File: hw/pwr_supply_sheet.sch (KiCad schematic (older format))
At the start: 17 parts

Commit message: starting to redraw the pcb as a smaller (icu enclosure)
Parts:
- C201, C205: symbol 100nF -> kemet:100nF
- C202: symbol CAP_EEE-FK1H470P -> usevolt:CAP_EEE-FK1H470P
- C203: symbol 10nF -> kemet:10nF
- C204: symbol T491D226K035AT -> kemet:T491D226K035AT
- D201, D204: symbol DIODE_RS07J-GS18 -> usevolt:DIODE_RS07J-GS18
- D202, D205: symbol SCHOTTKY_DIODE_V40PW10C -> usevolt:SCHOTTKY_DIODE_V40PW10C
- D203: symbol DIODE_TVS_SMBJ33A-TRDO-214AA -> usevolt:DIODE_TVS_SMBJ33A-TRDO-214AA
- D206: symbol DIODE_TVS_TPSMD28A -> usevolt:DIODE_TVS_TPSMD28A
- F201: symbol FUSE_MC36211_350MA -> usevolt:FUSE_MC36211_350MA
- L201: symbol IND_744045210 -> usevolt:IND_744045210
- R201: symbol 10K -> yageo:10K
- R202: symbol 1K -> yageo:1K
- VR201: symbol LM2671SOIC8 -> usevolt:LM2671SOIC8
- VR202: symbol REG_MCP1700 -> usevolt:REG_MCP1700
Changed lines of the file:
@@
-EESchema Schematic File Version 2
-LIBS:esb-rescue
-LIBS:kemet
-LIBS:usevolt
-LIBS:wurth_elektronik_LED
-LIBS:power
-LIBS:yageo
+EESchema Schematic File Version 4
 LIBS:esb-cache
 EELAYER 26 0
@@
 VIN
 $Comp
-L FUSE_MC36211_350MA F201
+L usevolt:FUSE_MC36211_350MA F201
 U 1 1 57B8204F
 P 2500 3850
@@
 $EndComp
 $Comp
-L DIODE_TVS_SMBJ33A-TRDO-214AA D203
+L usevolt:DIODE_TVS_SMBJ33A-TRDO-214AA D203
 U 1 1 57B820C1
 P 2800 4050
@@
 $EndComp
 $Comp
-L 100nF C201
+L kemet:100nF C201
 U 1 1 57B8217A
 P 3400 3950
@@
 $EndComp
 $Comp
-L LM2671SOIC8 VR201
+L usevolt:LM2671SOIC8 VR201
 U 1 1 57B82261
 P 4850 4150
@@
 $EndComp
 $Comp
-L 10nF C203
+L kemet:10nF C203
 U 1 1 57B822C5
 P 5800 3950
@@
 $EndComp
 $Comp
-L DIODE_RS07J-GS18 D204
+L usevolt:DIODE_RS07J-GS18 D204
 U 1 1 57B82329
 P 6200 3950
@@
 $EndComp
 $Comp
-L 100nF C205
+L kemet:100nF C205
 U 1 1 57B82A3F
 P 8600 3950
@@
 $EndComp
 $Comp
-L +5V #PWR07
+L power:+5V #PWR07
 U 1 1 57B831F8
 P 6850 3600
@@
 $EndComp
 $Comp
-L +3V3 #PWR08
+L power:+3V3 #PWR08
 U 1 1 57B83259
 P 8600 3600
@@
 NoConn ~ 4550 4050
 $Comp
-L VDD #PWR09
+L power:VDD #PWR09
 U 1 1 57B9C56A
 P 3800 2100
@@
 $EndComp
 $Comp
-L PWR_FLAG #FLG010
+L power:PWR_FLAG #FLG010
 U 1 1 57B9C59C
 P 3800 2300
@@
 $EndComp
 $Comp
-L GND #PWR011
+L power:GND #PWR011
 U 1 1 57B9D351
 P 4300 2350
@@
 $EndComp
 $Comp
-L PWR_FLAG #FLG012
+L power:PWR_FLAG #FLG012
 U 1 1 57B9D3A1
 P 4300 2150
@@
 $EndComp
 $Comp
-L GND #PWR013
+L power:GND #PWR013
 U 1 1 57CF1F5E
 P 2800 5150
@@
 $EndComp
 $Comp
-L IND_744045210 L201
+L usevolt:IND_744045210 L201
 U 1 1 58945E39
 P 6500 3850
@@
 $EndComp
 $Comp
-L DIODE_RS07J-GS18 D201
+L usevolt:DIODE_RS07J-GS18 D201
 U 1 1 5896E2A2
 P 1900 3850
@@
 $EndComp
 $Comp
-L T491D226K035AT C204
+L kemet:T491D226K035AT C204
 U 1 1 597AF606
 P 6850 4050
@@
 $EndComp
 $Comp
-L REG_MCP1700 VR202
+L usevolt:REG_MCP1700 VR202
 U 1 1 597AF83E
 P 8000 3950
@@
 $EndComp
 $Comp
-L 10K R201
+L yageo:10K R201
 U 1 1 59B1277F
 P 1500 4350
@@
 $EndComp
 $Comp
-L 1K R202
+L yageo:1K R202
 U 1 1 59B12803
 P 1500 4750
@@
 $EndComp
 $Comp
-L GND #PWR014
+L power:GND #PWR014
 U 1 1 59B128CC
 P 1500 5000
@@
 VDD_SENSE
 $Comp
-L SCHOTTKY_DIODE_V40PW10C D202
+L usevolt:SCHOTTKY_DIODE_V40PW10C D202
 U 1 1 59B7B8B2
 P 2050 3250
@@
 $EndComp
 $Comp
-L SCHOTTKY_DIODE_V40PW10C D205
+L usevolt:SCHOTTKY_DIODE_V40PW10C D205
 U 1 1 59D9089A
 P 2050 2750
@@
 $EndComp
 $Comp
-L CAP_EEE-FK1H470P C202
+L usevolt:CAP_EEE-FK1H470P C202
 U 1 1 5A13B69C
 P 3800 4050
@@
 $EndComp
 $Comp
-L DIODE_TVS_TPSMD28A D206
+L usevolt:DIODE_TVS_TPSMD28A D206
 U 1 1 5A13BC8E
 P 2900 2950
@@
 $EndComp
 $Comp
-L GND #PWR015
+L power:GND #PWR015
 U 1 1 5A13BD77
 P 2900 3150

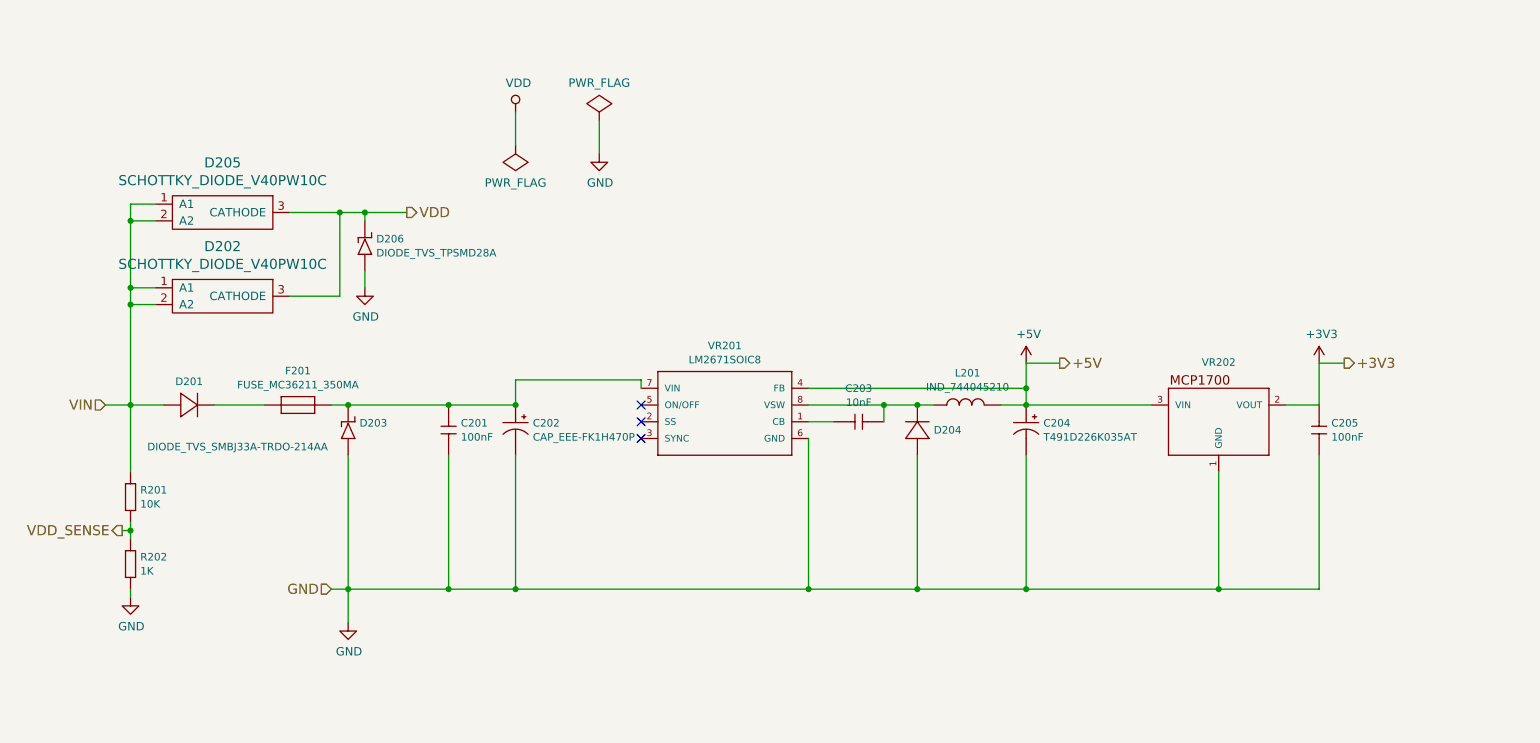
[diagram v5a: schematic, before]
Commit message: pump solenoid output working
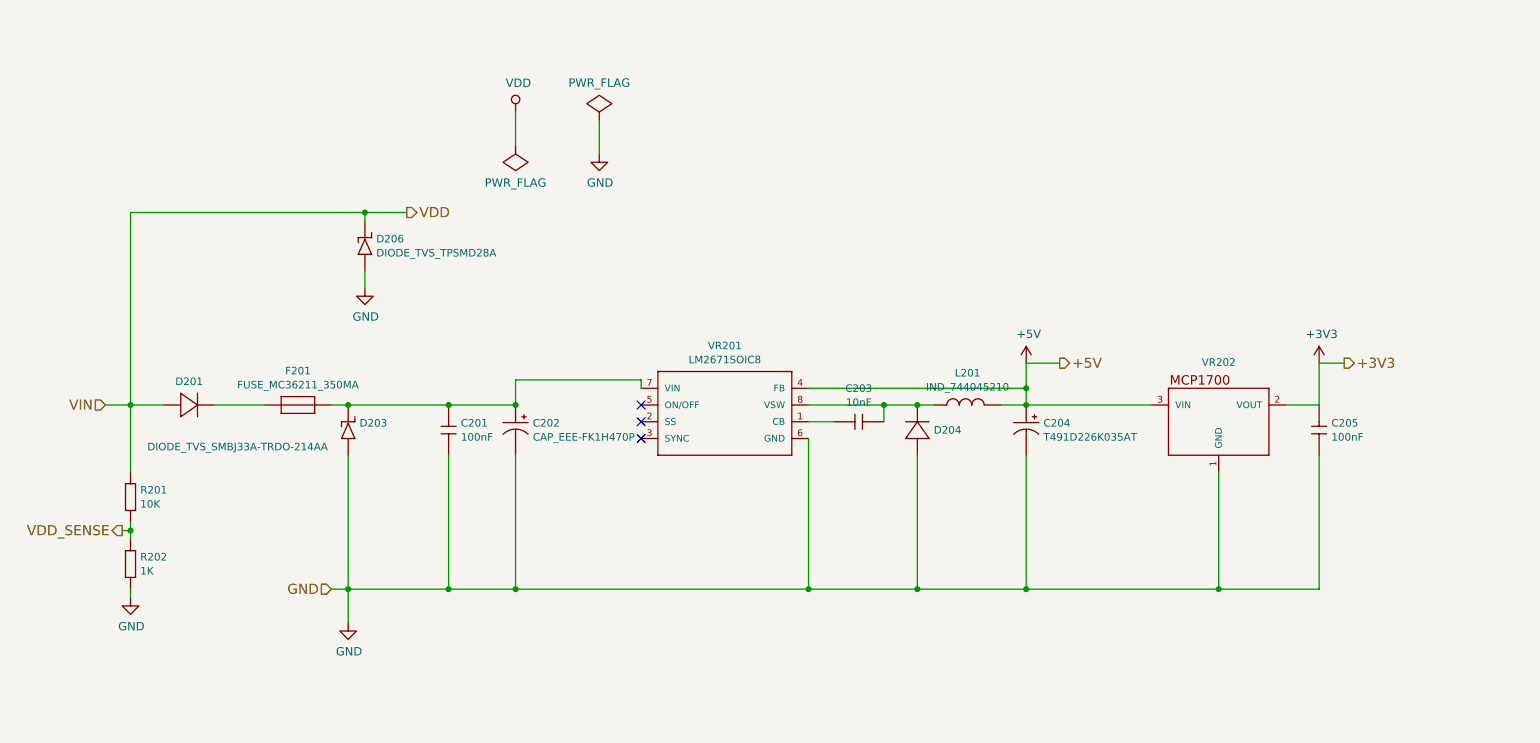
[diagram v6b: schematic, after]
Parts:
- removed D202, D205: SCHOTTKY_DIODE_V40PW10C, usevolt:SlimDPAK, symbol usevolt:SCHOTTKY_DIODE_V40PW10C
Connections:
- net VIN is gone; now on net VDD: D201.P$1 (P), R201.2 (R2)
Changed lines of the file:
@@
 VDD_SENSE
-$Comp
-L usevolt:SCHOTTKY_DIODE_V40PW10C D202
-U 1 1 59B7B8B2
-P 2050 3250
-F 0 "D202" H 2050 3597 60  0000 C CNN
-F 1 "SCHOTTKY_DIODE_V40PW10C" H 2050 3491 60  0000 C CNN
-F 2 "usevolt:SlimDPAK" H 1850 2900 60  0001 C CNN
-F 3 "http://www.farnell.com/datasheets/2245239.pdf?_ga=2.16591231.874534928.1505194133-1862443086.1504075057" H 1850 2900 60  0001 C CNN
-F 4 "2535169" H 2400 3850 60  0001 C CNN "1st Source Part Number"
-F 5 "Digikey" H 2500 3950 60  0001 C CNN "2nd Source"
-F 6 "Farnell" H 2300 3750 60  0001 C CNN "1st Source"
-F 7 "V40PW10CHM3/I" H 2200 3650 60  0001 C CNN "Manufacturer Part Number"
-F 8 "V40PW10CHM3/IGICT-ND" H 2600 4050 60  0001 C CNN "2nd Source Part Number"
-F 9 "VISHAY" H 2100 3550 60  0001 C CNN "Manufacturer"
-	1    2050 3250
-	1    0    0    -1
-$EndComp
-$Comp
-L usevolt:SCHOTTKY_DIODE_V40PW10C D205
-U 1 1 59D9089A
-P 2050 2750
-F 0 "D205" H 2050 3097 60  0000 C CNN
-F 1 "SCHOTTKY_DIODE_V40PW10C" H 2050 2991 60  0000 C CNN
-F 2 "usevolt:SlimDPAK" H 1850 2400 60  0001 C CNN
-F 3 "http://www.farnell.com/datasheets/2245239.pdf?_ga=2.16591231.874534928.1505194133-1862443086.1504075057" H 1850 2400 60  0001 C CNN
-F 4 "2535169" H 2400 3350 60  0001 C CNN "1st Source Part Number"
-F 5 "Digikey" H 2500 3450 60  0001 C CNN "2nd Source"
-F 6 "Farnell" H 2300 3250 60  0001 C CNN "1st Source"
-F 7 "V40PW10CHM3/I" H 2200 3150 60  0001 C CNN "Manufacturer Part Number"
-F 8 "V40PW10CHM3/IGICT-ND" H 2600 3550 60  0001 C CNN "2nd Source Part Number"
-F 9 "VISHAY" H 2100 3050 60  0001 C CNN "Manufacturer"
-	1    2050 2750
-	1    0    0    -1
-$EndComp
 $Comp
 L usevolt:CAP_EEE-FK1H470P C202
@@
 Connection ~ 3800 4950
 Wire Wire Line
-	2800 4150 2800 5150
+	2800 4150 2800 4950
 Connection ~ 3400 4950
 Connection ~ 2800 3850
@@
 	8600 3850 8400 3850
 Wire Wire Line
-	6700 3850 7600 3850
+	6700 3850 6850 3850
 Connection ~ 6850 3850
 Wire Wire Line
-	5550 3850 6300 3850
+	5550 3850 6000 3850
 Connection ~ 6200 3850
 Wire Wire Line
@@
 	5550 3750 6850 3750
 Wire Wire Line
-	6850 3600 6850 3850
+	6850 3600 6850 3750
 Connection ~ 6850 3750
 Wire Wire Line
-	1350 3850 1700 3850
+	1350 3850 1500 3850
 Wire Wire Line
 	3800 3700 4550 3700
@@
 Connection ~ 1500 3850
 Wire Wire Line
-	2700 3850 3800 3850
+	2700 3850 2800 3850
 Wire Wire Line
 	2000 3850 2300 3850
 Wire Wire Line
-	2700 4950 8600 4950
+	2700 4950 2800 4950
 Wire Wire Line
 	1500 5000 1500 4950
 Wire Wire Line
-	1500 4550 1500 4650
+	1500 4550 1500 4600
 Wire Wire Line
 	1500 4600 1450 4600
 Connection ~ 1500 4600
-Wire Wire Line
-	2750 3200 2450 3200
-Wire Wire Line
-	1500 2650 1500 4250
-Wire Wire Line
-	1500 3150 1650 3150
-Wire Wire Line
-	1650 3250 1500 3250
-Connection ~ 1500 3250
-Wire Wire Line
-	1500 2750 1650 2750
-Connection ~ 1500 3150
-Wire Wire Line
-	1500 2650 1650 2650
-Connection ~ 1500 2750
-Wire Wire Line
-	2450 2700 3150 2700
-Wire Wire Line
-	2750 2700 2750 3200
 Connection ~ 3800 3850
-Connection ~ 2750 2700
 Wire Wire Line
 	2900 2750 2900 2700
-Connection ~ 2900 2700
 Wire Wire Line
 	2900 3150 2900 3050
+Wire Wire Line
+	8000 4950 8600 4950
+Wire Wire Line
+	6850 4950 8000 4950
+Wire Wire Line
+	6200 4950 6850 4950
+Wire Wire Line
+	5550 4950 6200 4950
+Wire Wire Line
+	3800 4950 5550 4950
+Wire Wire Line
+	3400 4950 3800 4950
+Wire Wire Line
+	2800 3850 3400 3850
+Wire Wire Line
+	3400 3850 3800 3850
+Wire Wire Line
+	6850 3850 7600 3850
+Wire Wire Line
+	6200 3850 6300 3850
+Wire Wire Line
+	6000 3850 6200 3850
+Wire Wire Line
+	6850 3750 6850 3850
+Wire Wire Line
+	2800 4950 2800 5150
+Wire Wire Line
+	2800 4950 3400 4950
+Wire Wire Line
+	1500 3850 1700 3850
+Wire Wire Line
+	1500 3850 1500 4250
+Wire Wire Line
+	1500 4600 1500 4650
+Wire Wire Line
+	2900 2700 3150 2700
+Wire Wire Line
+	1500 2700 1500 3850
+Wire Wire Line
+	1500 2700 2900 2700
+Connection ~ 2900 2700
 $EndSCHEMATC

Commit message: pcb 5.2.0 ready for order, with radiator power output
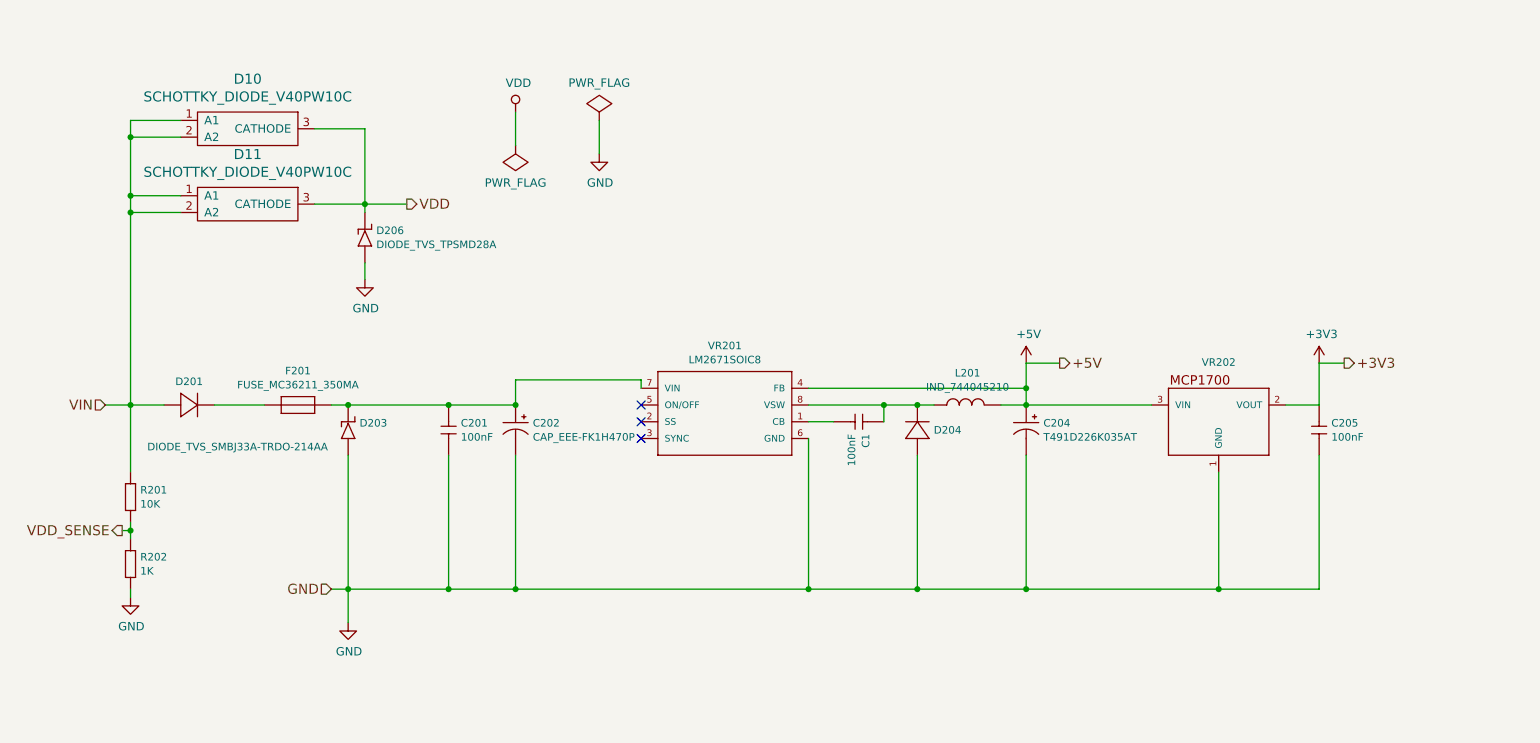
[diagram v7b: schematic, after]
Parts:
- removed C203: 10nF, kemet:0603, symbol kemet:10nF
- added C1: 100nF, kemet:0603, symbol kemet:100nF
- added D10, D11: SCHOTTKY_DIODE_V40PW10C, usevolt:SlimDPAK, symbol usevolt:SCHOTTKY_DIODE_V40PW10C
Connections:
- net VDD: now also D10.3 (CATHODE), D11.3 (CATHODE); no longer D201.P$1 (P), R201.2 (R2)
- net at VR201.1 (CB): now also C1.2 (C2)
- net at D204.P$2 (N), L201.1, VR201.8 (VSW): now also C1.1 (C1)
- new net VIN: D10.1 (A1), D10.2 (A2), D11.1 (A1), D11.2 (A2), D201.P$1 (P), R201.2 (R2)
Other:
- moved on the sheet: D206
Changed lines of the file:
@@
-$EndComp
-$Comp
-L kemet:10nF C203
-U 1 1 57B822C5
-P 5800 3950
-F 0 "C203" H 5850 4149 45  0000 C CNN
-F 1 "10nF" H 5850 4065 45  0000 C CNN
-F 2 "kemet:0603" H 5830 4100 20  0001 C CNN
-F 3 "http://www.farnell.com/datasheets/2064086.pdf?_ga=1.250530118.1948984246.1460023966" H 5704 3959 60  0001 C CNN
-F 4 "1457729" H 6104 4359 60  0001 C CNN "1st Source Part Number"
-F 5 "C0603C103J3GACTU" H 5904 4159 60  0001 C CNN "Manufacturer Part Number"
-F 6 "Farnell" H 6004 4259 60  0001 C CNN "1st Source"
-F 7 "KEMET" H 5804 4059 60  0001 C CNN "Manufacturer"
-	1    5800 3950
-	1    0    0    -1
 $EndComp
 $Comp
@@
 Text HLabel 8750 3600 2    60   Output ~ 0
 +3V3
-Text HLabel 3150 2700 2    60   Output ~ 0
+Text HLabel 3150 2650 2    60   Output ~ 0
 VDD
 Text HLabel 2700 4950 0    60   Input ~ 0
@@
 L usevolt:DIODE_TVS_TPSMD28A D206
 U 1 1 5A13BC8E
-P 2900 2950
-F 0 "D206" V 2992 2882 45  0000 R CNN
-F 1 "DIODE_TVS_TPSMD28A" V 2908 2882 45  0000 R CNN
-F 2 "usevolt:DO-214AB" H 2930 3100 20  0001 C CNN
-F 3 "http://www.littelfuse.com/~/media/electronics/datasheets/tvs_diodes/littelfuse_tvs_diode_tpsmd_datasheet.pdf.pdf" H 3010 2960 60  0001 C CNN
-F 4 "Digi-Key" H 3310 3260 60  0001 C CNN "1st Source"
-F 5 "Littlefuse" H 3110 3060 60  0001 C CNN "Manufacturer"
-F 6 "TPSMD28A" H 3210 3160 60  0001 C CNN "Manufacturer Part Number"
-F 7 "F6570CT-ND" H 3410 3360 60  0001 C CNN "1st Source Part Number"
-	1    2900 2950
+P 2900 2900
+F 0 "D206" V 2992 2832 45  0000 R CNN
+F 1 "DIODE_TVS_TPSMD28A" V 2908 2832 45  0000 R CNN
+F 2 "usevolt:DO-214AB" H 2930 3050 20  0001 C CNN
+F 3 "http://www.littelfuse.com/~/media/electronics/datasheets/tvs_diodes/littelfuse_tvs_diode_tpsmd_datasheet.pdf.pdf" H 3010 2910 60  0001 C CNN
+F 4 "Digi-Key" H 3310 3210 60  0001 C CNN "1st Source"
+F 5 "Littlefuse" H 3110 3010 60  0001 C CNN "Manufacturer"
+F 6 "TPSMD28A" H 3210 3110 60  0001 C CNN "Manufacturer Part Number"
+F 7 "F6570CT-ND" H 3410 3310 60  0001 C CNN "1st Source Part Number"
+	1    2900 2900
 	0    -1   -1   0
 $EndComp
@@
 L power:GND #PWR015
 U 1 1 5A13BD77
-P 2900 3150
-F 0 "#PWR015" H 2900 2900 50  0001 C CNN
-F 1 "GND" H 2905 2977 50  0000 C CNN
-F 2 "" H 2900 3150 50  0000 C CNN
-F 3 "" H 2900 3150 50  0000 C CNN
-	1    2900 3150
+P 2900 3100
+F 0 "#PWR015" H 2900 2850 50  0001 C CNN
+F 1 "GND" H 2905 2927 50  0000 C CNN
+F 2 "" H 2900 3100 50  0000 C CNN
+F 3 "" H 2900 3100 50  0000 C CNN
+	1    2900 3100
 	1    0    0    -1
 $EndComp
@@
 Connection ~ 3800 3850
 Wire Wire Line
-	2900 2750 2900 2700
-Wire Wire Line
-	2900 3150 2900 3050
+	2900 2700 2900 2650
+Wire Wire Line
+	2900 3100 2900 3000
 Wire Wire Line
 	8000 4950 8600 4950
@@
 	1500 4600 1500 4650
 Wire Wire Line
-	2900 2700 3150 2700
+	2900 2650 3150 2650
+$Comp
+L usevolt:SCHOTTKY_DIODE_V40PW10C D10
+U 1 1 5C521B18
+P 2200 2250
+F 0 "D10" H 2200 2597 60  0000 C CNN
+F 1 "SCHOTTKY_DIODE_V40PW10C" H 2200 2491 60  0000 C CNN
+F 2 "usevolt:SlimDPAK" H 2000 1900 60  0001 C CNN
+F 3 "http://www.farnell.com/datasheets/2245239.pdf?_ga=2.16591231.874534928.1505194133-1862443086.1504075057" H 2000 1900 60  0001 C CNN
+F 4 "2535169" H 2550 2850 60  0001 C CNN "1st Source Part Number"
+F 5 "Digikey" H 2650 2950 60  0001 C CNN "2nd Source"
+F 6 "Farnell" H 2450 2750 60  0001 C CNN "1st Source"
+F 7 "V40PW10CHM3/I" H 2350 2650 60  0001 C CNN "Manufacturer Part Number"
+F 8 "V40PW10CHM3/IGICT-ND" H 2750 3050 60  0001 C CNN "2nd Source Part Number"
+F 9 "VISHAY" H 2250 2550 60  0001 C CNN "Manufacturer"
+	1    2200 2250
+	1    0    0    -1
+$EndComp
+$Comp
+L usevolt:SCHOTTKY_DIODE_V40PW10C D11
+U 1 1 5C5227A8
+P 2200 2700
+F 0 "D11" H 2200 3047 60  0000 C CNN
+F 1 "SCHOTTKY_DIODE_V40PW10C" H 2200 2941 60  0000 C CNN
+F 2 "usevolt:SlimDPAK" H 2000 2350 60  0001 C CNN
+F 3 "http://www.farnell.com/datasheets/2245239.pdf?_ga=2.16591231.874534928.1505194133-1862443086.1504075057" H 2000 2350 60  0001 C CNN
+F 4 "2535169" H 2550 3300 60  0001 C CNN "1st Source Part Number"
+F 5 "Digikey" H 2650 3400 60  0001 C CNN "2nd Source"
+F 6 "Farnell" H 2450 3200 60  0001 C CNN "1st Source"
+F 7 "V40PW10CHM3/I" H 2350 3100 60  0001 C CNN "Manufacturer Part Number"
+F 8 "V40PW10CHM3/IGICT-ND" H 2750 3500 60  0001 C CNN "2nd Source Part Number"
+F 9 "VISHAY" H 2250 3000 60  0001 C CNN "Manufacturer"
+	1    2200 2700
+	1    0    0    -1
+$EndComp
+Wire Wire Line
+	1500 2150 1800 2150
+Wire Wire Line
+	1500 2150 1500 2250
+Wire Wire Line
+	1800 2250 1500 2250
+Connection ~ 1500 2250
+Wire Wire Line
+	1500 2250 1500 2600
+Wire Wire Line
+	1800 2600 1500 2600
+Connection ~ 1500 2600
+Wire Wire Line
+	1500 2600 1500 2700
+Wire Wire Line
+	1800 2700 1500 2700
+Connection ~ 1500 2700
 Wire Wire Line
 	1500 2700 1500 3850
 Wire Wire Line
-	1500 2700 2900 2700
-Connection ~ 2900 2700
+	2600 2650 2900 2650
+Connection ~ 2900 2650
+Wire Wire Line
+	2900 2650 2900 2200
+Wire Wire Line
+	2900 2200 2600 2200
+$Comp
+L kemet:100nF C1
+U 1 1 5C52E6DA
+P 5900 3950
+F 0 "C1" V 5908 4023 45  0000 L CNN
+F 1 "100nF" V 5992 4023 45  0000 L CNN
+F 2 "kemet:0603" H 5930 4100 20  0001 C CNN
+F 3 "http://www.farnell.com/datasheets/2062872.pdf?_ga=1.250530118.1948984246.1460023966" H 5804 3959 60  0001 C CNN
+F 4 "1288255" H 6204 4359 60  0001 C CNN "1st Source Part Number"
+F 5 "C0603C104K5RACTU" H 6004 4159 60  0001 C CNN "Manufacturer Part Number"
+F 6 "Farnell" H 6104 4259 60  0001 C CNN "1st Source"
+F 7 "KEMET" H 5904 4059 60  0001 C CNN "Manufacturer"
+	1    5900 3950
+	-1   0    0    1
+$EndComp
 $EndSCHEMATC
